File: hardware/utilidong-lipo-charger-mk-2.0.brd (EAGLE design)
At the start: 32 x 30 mm, 31 parts, among them IC1 LT1610, IC2 MCP73831, Q1 N-MOSFET

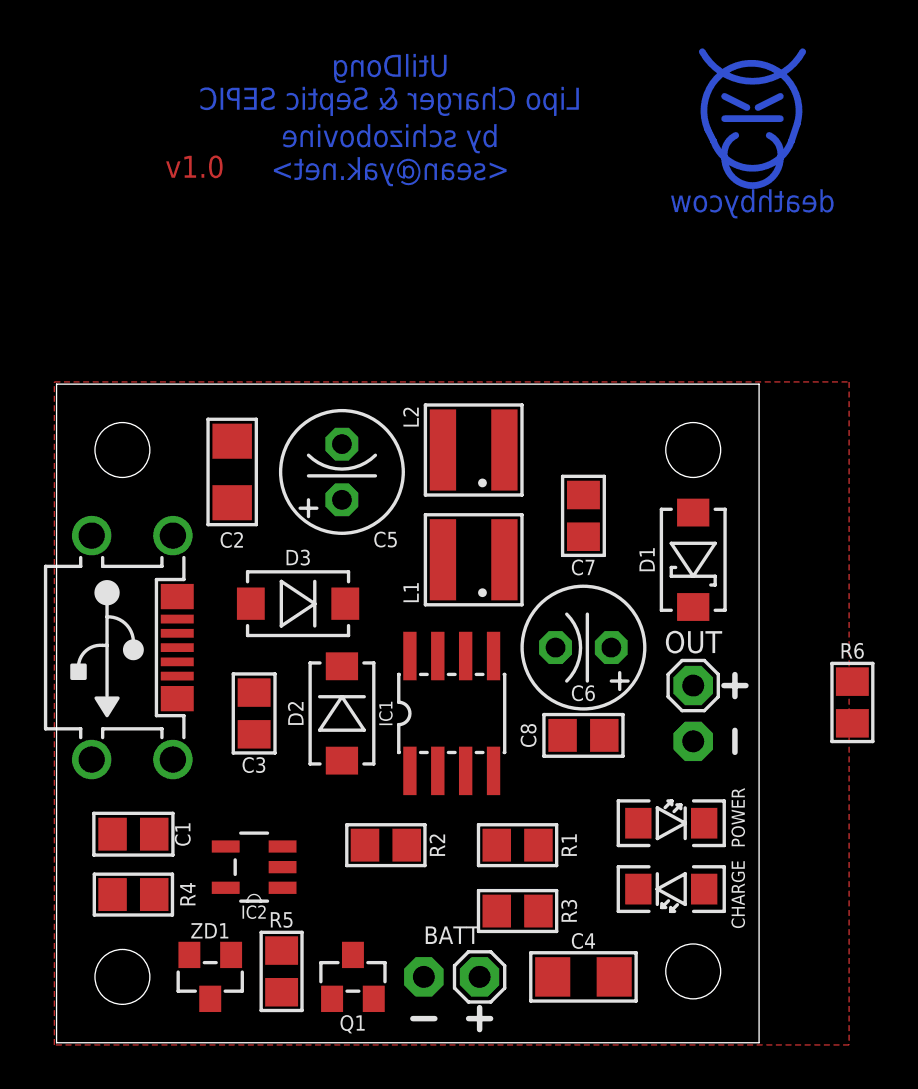
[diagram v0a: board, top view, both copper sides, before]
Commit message: new version of lipo charger with system load balancing
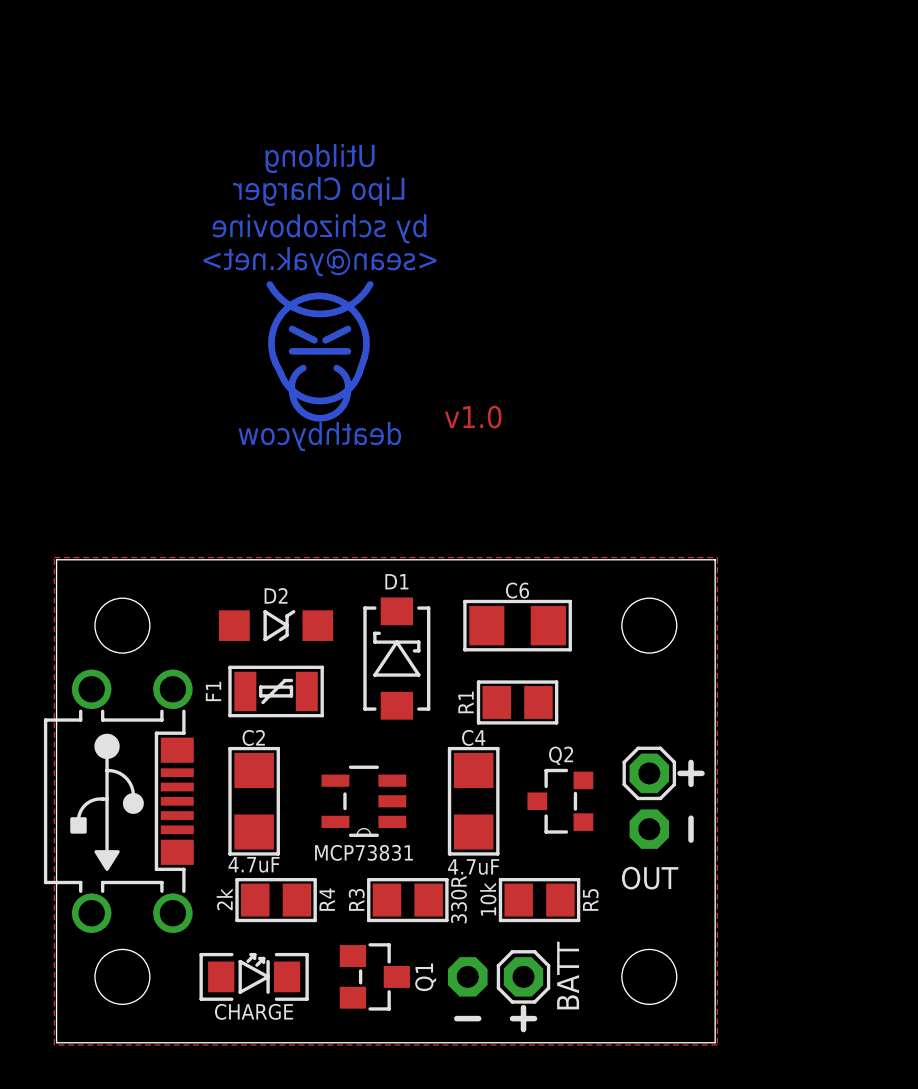
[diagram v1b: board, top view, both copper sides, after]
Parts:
- removed C1, C3: 100nF, A_butts:C0805
- removed C5: 22uF, A_butts:E2,5-6
- removed C7, C8: 1uF, A_butts:C0805
- removed D3: MBRA140, A_butts:SMA-DIODE
- removed IC1: LT1610, A_butts:SO08
- removed IC2: MCP73831, A_butts:SOT95P280X145-5N
- removed L1, L2: 22uH, A_butts:TAIYO-YUDEN-40XX
- removed POWER: LED1206, A_butts:LED-1206
- removed R2: 604k, A_butts:R0805
- removed R6: 330R, A_butts:R0805
- removed ZD1: 10V, A_butts:SOT23
- added F1: PTCSMD, A_butts:PTC-1206
- added Q2: IRLML2244, A_butts:SOT23-3
- added U1: MCP73831, A_butts:SOT95P280X145-5N
- C2, C4: value 10uF -> 4.7uF
- C6: value 22uF -> 4.7uF; device A_butts:E2,5-6 -> A_butts:C1206
- D1: value MBRA140 -> MBR140
- D2: value MBRA140 -> MMSZ5232B; device A_butts:SMA-DIODE -> A_butts:SOD123-ZENER
- Q1: value N-MOSFET -> IRLML2502
- R1: value 1M -> 10k
- moved U$9 22.4 mm to (12.0, 32.0)
- moved U$8 19.9 mm to (12.0, 25.0)
- moved CHARGE 19.4 mm to (9.00, 3.00), turned to 0 degrees
- moved C2 15.0 mm to (9.00, 11.0), turned to 270 degrees
- moved D1 14.2 mm to (15.5, 17.5), turned to 90 degrees
- moved R5 12.2 mm to (22.0, 6.50), turned to 180 degrees
- moved C4 9.43 mm to (19.0, 11.0), turned to 270 degrees
- moved USB1 7.00 mm to (5.50, 11.0)
- moved R4 6.50 mm to (10.0, 6.50)
- moved R1 6.50 mm to (21.0, 15.5), turned to 0 degrees
- moved R3 5.02 mm to (16.0, 6.50), turned to 0 degrees
- moved D2 5.00 mm to (10.0, 19.0), turned to 0 degrees
- moved OUT 4.47 mm to (27.0, 11.0)
- moved C6 3.16 mm to (21.0, 19.0)
- moved BATT 2.00 mm to (20.0, 3.00)
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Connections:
- removed net N$1: C7.1, D1.A, L2.1
- removed net N$3: POWER.A, R6.2
- removed net N$4: IC1.1, IC1.8
- removed net N$7: IC1.2, R1.2, R2.1
- removed net VIN: C5.+, D2.C, D3.C, IC1.3, IC1.6, L1.2
- net 5V: now also D1.A, D2.C, F1.2, Q2.1, R1.1, U1.4; no longer C1.1, D3.A, IC2.4, USB1.1
- net GND: now also C6.2, D2.A, R1.2, U1.2; no longer C1.2, C3.2, C5.-, C6.-, C8.2, IC1.4, IC1.7, IC2.2, L2.2, POWER.C, R2.2, ZD1.1, ZD1.2
- net N$11: no longer ZD1.3
- net N$2: now also F1.1, USB1.1; no longer C7.2, IC1.5, L1.1
- net N$5: now also U1.1; no longer IC2.1
- net N$8: now also U1.5; no longer IC2.5
- net VBATT+: now also Q2.3, U1.3; no longer C3.1, D2.A, IC2.3
- net VOUT: now also C6.1, Q2.2; no longer C6.+, C8.1, R1.1, R6.1
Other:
- board size 32 x 30 mm -> 30 x 22 mm
- board text added: "Utildong Lipo Charger"
- board text removed: "UtilDong Lipo Charger & Septic SEPIC"
